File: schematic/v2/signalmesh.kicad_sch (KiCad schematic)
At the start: 37 parts, among them J13 UUM_DBG, U21 74HC4050D, U22 AP2112K-3.3, U23 W25Q128JVS, U24 74HC4050D, U25 AP2112K-3.3, U26 W25Q128JVS, U27 MCP2551-I-P, U28 74LVC1G3157, U29 MCP2551-I-P, U3 NUCLEO-F303RE, U30 MCP2551-I-P, U31 MCP2551-I-P

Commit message: no errors in the ERC!
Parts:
- removed C10: 0.1uf, Capacitor_SMD:C_0805_2012Metric, symbol Device:C_Small
- removed C8, C9: 10uf, Capacitor_SMD:C_0805_2012Metric, symbol Device:C_Small
- removed D25, D26, D27, D28: LED_PWR, LED_SMD:LED_0603_1608Metric, symbol Device:LED
- removed D29: LED_OK, LED_SMD:LED_0603_1608Metric, symbol Device:LED
- removed D30: LED_FAIL, LED_SMD:LED_0603_1608Metric, symbol Device:LED
- removed D31: LED_WARN, LED_SMD:LED_0603_1608Metric, symbol Device:LED
- removed J13: UUM_DBG, Connector_PinHeader_1.00mm:PinHeader_1x03_P1.00mm_Horizontal, symbol Connector_Generic:Conn_01x03
- removed R10, R43, R45, R46, R48, R49, R9: 300, Resistor_SMD:R_0805_2012Metric_Pad1.20x1.40mm_HandSolder, symbol Device:R
- removed R42: 100, Resistor_SMD:R_0805_2012Metric_Pad1.20x1.40mm_HandSolder, symbol Device:R
- removed U21, U24: 74HC4050D, 74HC4050D:SO16, symbol 74HC4050D:74HC4050D
- removed U22, U25: AP2112K-3.3, Package_TO_SOT_SMD:SOT-23-5, symbol Regulator_Linear:AP2112K-3.3
- removed U23, U26: W25Q128JVS, Package_SO:SOIC-8_5.3x5.3mm_P1.27mm, symbol Memory_Flash:W25Q128JVS
- removed U28: 74LVC1G3157, SN74LVC1G3157:SC70-6, symbol 74xGxx:74LVC1G3157
- removed U3: NUCLEO-F303RE, NUCLEO-F303RE:ST_NUCLEO-F303RE, symbol NUCLEO-F303RE:NUCLEO-F303RE
- added R73, R74, R75, R76: 10k, Resistor_SMD:R_0805_2012Metric_Pad1.20x1.40mm_HandSolder, symbol Device:R
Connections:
- net VDD_UUM is gone; now on net UUM_VDD: U27.3 (VDD)
- net GND: now also R73.2, R74.2, R75.2, R76.2
- net at U31.8 (Rs): now also R76.1
- net at U27.8 (Rs): now also R73.1
- net at U29.8 (Rs): now also R74.1
- net at U30.8 (Rs): now also R75.1
- net VDD_APM renamed APM_VDD
- net VDD_DSM renamed DSM_VDD
- net VDD_TDM renamed TDM_VDD
- no-connect marks 0 -> 4
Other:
- added sheet UUM (UUM.kicad_sch)
- sheet TDM ports: added 7SDD_VDD, APM_VDD, DSM_VDD, TDM_VDD, UUM_VDD; removed none
- note removed: "UUM writes to both SPI flashes at once but can only read from 1 at a time via a GPIO-ctrl'd switch"
- note removed: "Upload & Update Module"
- note removed: "W25Q128 UUM #1"
- note removed: "W25Q128 UUM #2"
- moved on the sheet: H1, H2, H5, H6, R44, R47, U27, U29, U30, U31

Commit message: attempting new PCB layout
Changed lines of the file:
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@@
 	(wire
 		(pts
-			(xy 185.42 186.69) (xy 198.12 186.69)
+			(xy 102.87 185.42) (xy 115.57 185.42)
 		)
 		(stroke
@@
 	(wire
 		(pts
-			(xy 185.42 208.28) (xy 198.12 208.28)
+			(xy 181.61 165.1) (xy 194.31 165.1)
 		)
 		(stroke
@@
 	(wire
 		(pts
-			(xy 185.42 184.15) (xy 198.12 184.15)
+			(xy 102.87 182.88) (xy 115.57 182.88)
 		)
 		(stroke
@@
 	(wire
 		(pts
-			(xy 185.42 210.82) (xy 198.12 210.82)
+			(xy 181.61 167.64) (xy 194.31 167.64)
 		)
 		(stroke
@@
 	)
 	(label "TDM_CAN_RD"
-		(at 185.42 184.15 0)
+		(at 102.87 182.88 0)
 		(effects
 			(font
@@
 	)
 	(label "UUM_CAN_RD"
-		(at 185.42 208.28 0)
+		(at 181.61 165.1 0)
 		(effects
 			(font
@@
 	)
 	(label "UUM_CAN_TD"
-		(at 185.42 210.82 0)
+		(at 181.61 167.64 0)
 		(effects
 			(font
@@
 	)
 	(label "TDM_CAN_TD"
-		(at 185.42 186.69 0)
+		(at 102.87 185.42 0)
 		(effects
 			(font
@@
 	)
 	(sheet
-		(at 198.12 162.56)
-		(size 31.75 27.94)
+		(at 115.57 161.29)
+		(size 38.1 27.94)
 		(exclude_from_sim no)
 		(in_bom yes)
@@
 		)
 		(property "Sheetname" "TDM"
-			(at 198.12 161.8484 0)
+			(at 115.57 160.5784 0)
 			(effects
 				(font
@@
 		)
 		(property "Sheetfile" "TDM.kicad_sch"
-			(at 198.12 191.0846 0)
+			(at 115.57 189.8146 0)
 			(effects
 				(font
@@
 		)
 		(property "Field2" ""
-			(at 198.12 162.56 0)
+			(at 115.57 161.29 0)
 			(effects
 				(font
@@
 		)
 		(pin "TDM_CAN_TD" output
-			(at 198.12 186.69 180)
+			(at 115.57 185.42 180)
 			(effects
 				(font
@@
 		)
 		(pin "TDM_CAN_RD" input
-			(at 198.12 184.15 180)
+			(at 115.57 182.88 180)
 			(effects
 				(font
@@
 		)
 		(pin "UUM_VDD" output
-			(at 229.87 179.07 0)
+			(at 153.67 177.8 0)
 			(effects
 				(font
@@
 		)
 		(pin "ACM_VDD" output
-			(at 229.87 168.91 0)
+			(at 153.67 167.64 0)
 			(effects
 				(font
@@
 		)
 		(pin "7SDD_VDD" output
-			(at 229.87 166.37 0)
+			(at 153.67 165.1 0)
 			(effects
 				(font
@@
 		)
 		(pin "TDM_VDD" output
-			(at 229.87 176.53 0)
+			(at 153.67 175.26 0)
 			(effects
 				(font
@@
 		)
 		(pin "APM_VDD" output
-			(at 229.87 171.45 0)
+			(at 153.67 170.18 0)
 			(effects
 				(font
@@
 		)
 		(pin "DSM_VDD" output
-			(at 229.87 173.99 0)
+			(at 153.67 172.72 0)
 			(effects
 				(font
@@
 	)
 	(sheet
-		(at 198.12 204.47)
-		(size 31.75 12.7)
+		(at 194.31 161.29)
+		(size 38.1 27.94)
 		(exclude_from_sim no)
 		(in_bom yes)
@@
 		)
 		(property "Sheetname" "UUM"
-			(at 198.12 203.7584 0)
+			(at 194.31 160.5784 0)
 			(effects
 				(font
@@
 		)
 		(property "Sheetfile" "UUM.kicad_sch"
-			(at 198.12 217.7546 0)
+			(at 194.31 189.8146 0)
 			(effects
 				(font
@@
 		)
 		(pin "UUM_CAN_RD" input
-			(at 198.12 208.28 180)
+			(at 194.31 165.1 180)
 			(effects
 				(font
@@
 		)
 		(pin "UUM_CAN_TD" output
-			(at 198.12 210.82 180)
+			(at 194.31 167.64 180)
 			(effects
 				(font

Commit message: time to start routing?
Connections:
- no-connect marks 4 -> 9
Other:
- added sheet USB_debug_ACM (USB_debug.kicad_sch)
- added sheet USB_debug_APM (USB_debug.kicad_sch)
- added sheet USB_debug_DSM (USB_debug.kicad_sch)
- added sheet USB_debug_TDM (USB_debug.kicad_sch)
- added sheet USB_debug_UUM (USB_debug.kicad_sch)
- sheet ACM ports: added ACM_DBG_RX, ACM_DBG_TX, ACM_VDD; removed none
- sheet APM ports: added APM_DBG_RX, APM_DBG_TX, APM_VDD; removed none
- sheet DSM ports: added DSM_DBG_RX, DSM_DBG_TX, DSM_VDD; removed none
- sheet TDM ports: added TDM_DBG_RX, TDM_DBG_TX; removed none
- sheet UUM ports: added UUM_DBG_RX, UUM_DBG_TX, UUM_VDD; removed none
- moved on the sheet: R44, R47, R73, R74, R75, R76, U27, U29, U30, U31

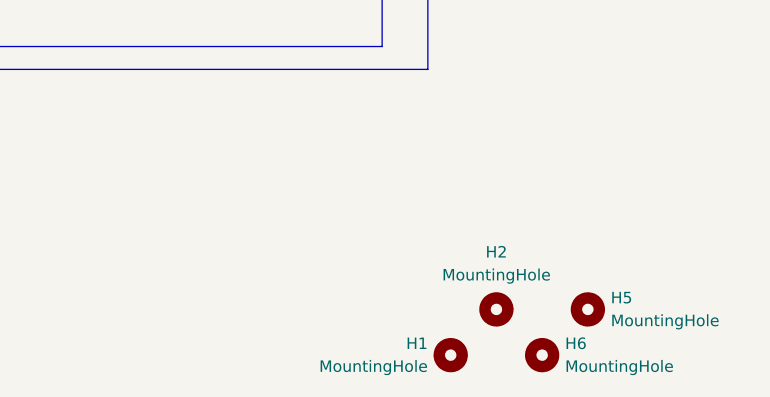
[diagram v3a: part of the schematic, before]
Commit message: gonna throw auto route on. I think I have enough put together for now
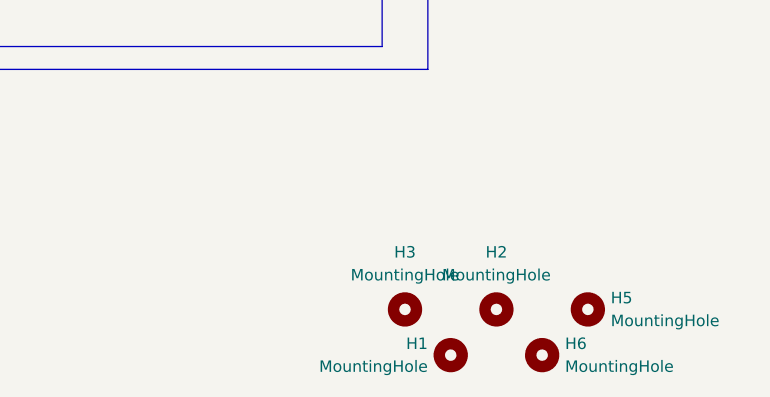
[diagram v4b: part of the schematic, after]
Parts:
- added H3: MountingHole, MountingHole:MountingHole_3.2mm_M3, symbol Mechanical:MountingHole
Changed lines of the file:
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@@
+	)
+	(symbol
+		(lib_id "Mechanical:MountingHole")
+		(at 372.11 243.84 0)
+		(unit 1)
+		(exclude_from_sim no)
+		(in_bom no)
+		(on_board yes)
+		(dnp no)
+		(fields_autoplaced yes)
+		(property "Reference" "H3"
+			(at 372.11 237.49 0)
+			(effects
+				(font
+					(size 1.27 1.27)
+				)
+			)
+		)
+		(property "Value" "MountingHole"
+			(at 372.11 240.03 0)
+			(effects
+				(font
+					(size 1.27 1.27)
+				)
+			)
+		)
+		(property "Footprint" "MountingHole:MountingHole_3.2mm_M3"
+			(at 372.11 243.84 0)
+			(effects
+				(font
+					(size 1.27 1.27)
+				)
+				(hide yes)
+			)
+		)
+		(property "Datasheet" "~"
+			(at 372.11 243.84 0)
+			(effects
+				(font
+					(size 1.27 1.27)
+				)
+				(hide yes)
+			)
+		)
+		(property "Description" "Mounting Hole without connection"
+			(at 372.11 243.84 0)
+			(effects
+				(font
+					(size 1.27 1.27)
+				)
+				(hide yes)
+			)
+		)
+		(instances
+			(project "signalmesh"
+				(path "/fe7b15e9-f0ed-4338-9f03-dd7651dace13"
+					(reference "H3")
+					(unit 1)
+				)
+			)
+		)
 	)
 	(symbol

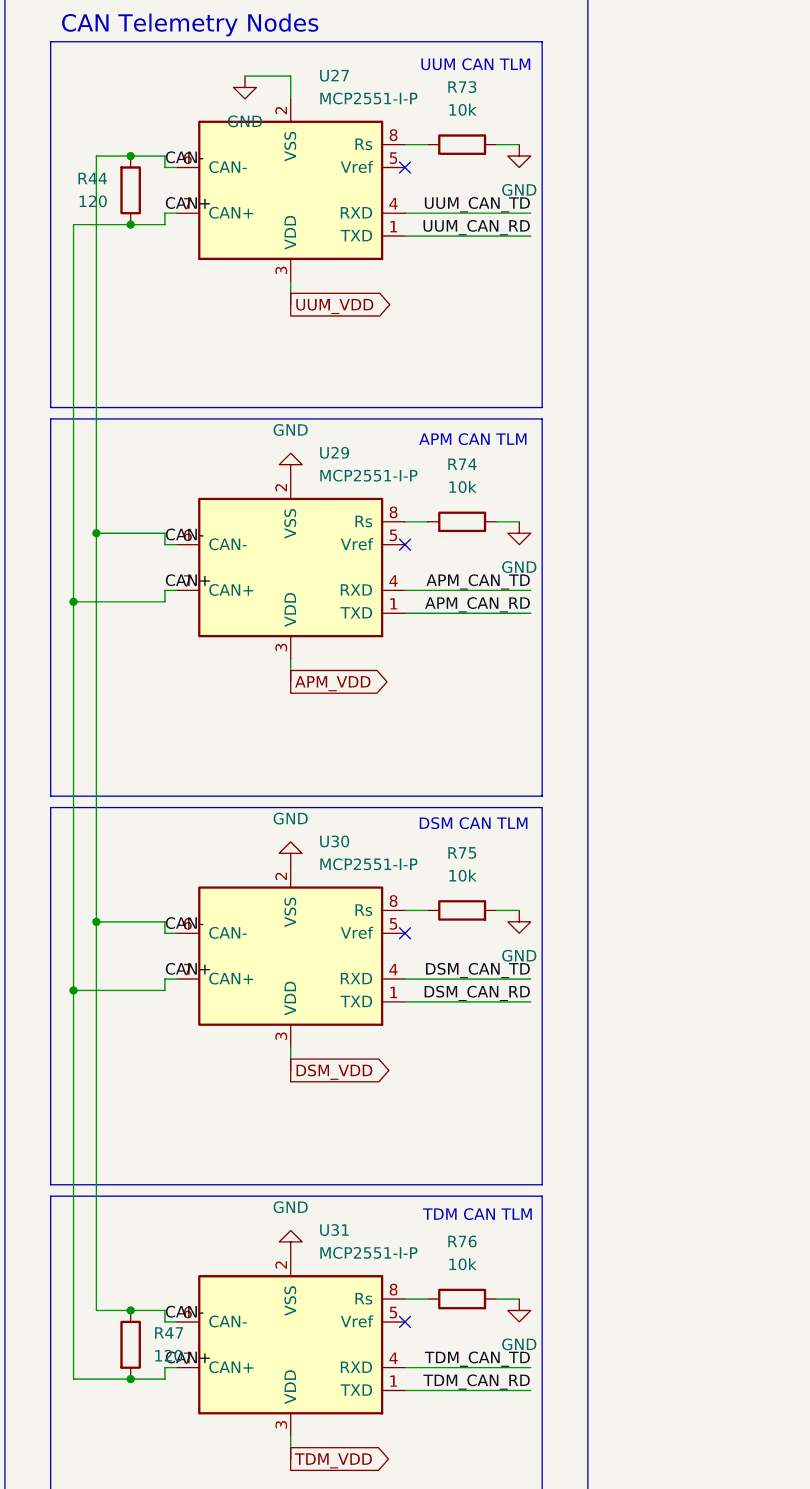
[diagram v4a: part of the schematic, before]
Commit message: fixed designators
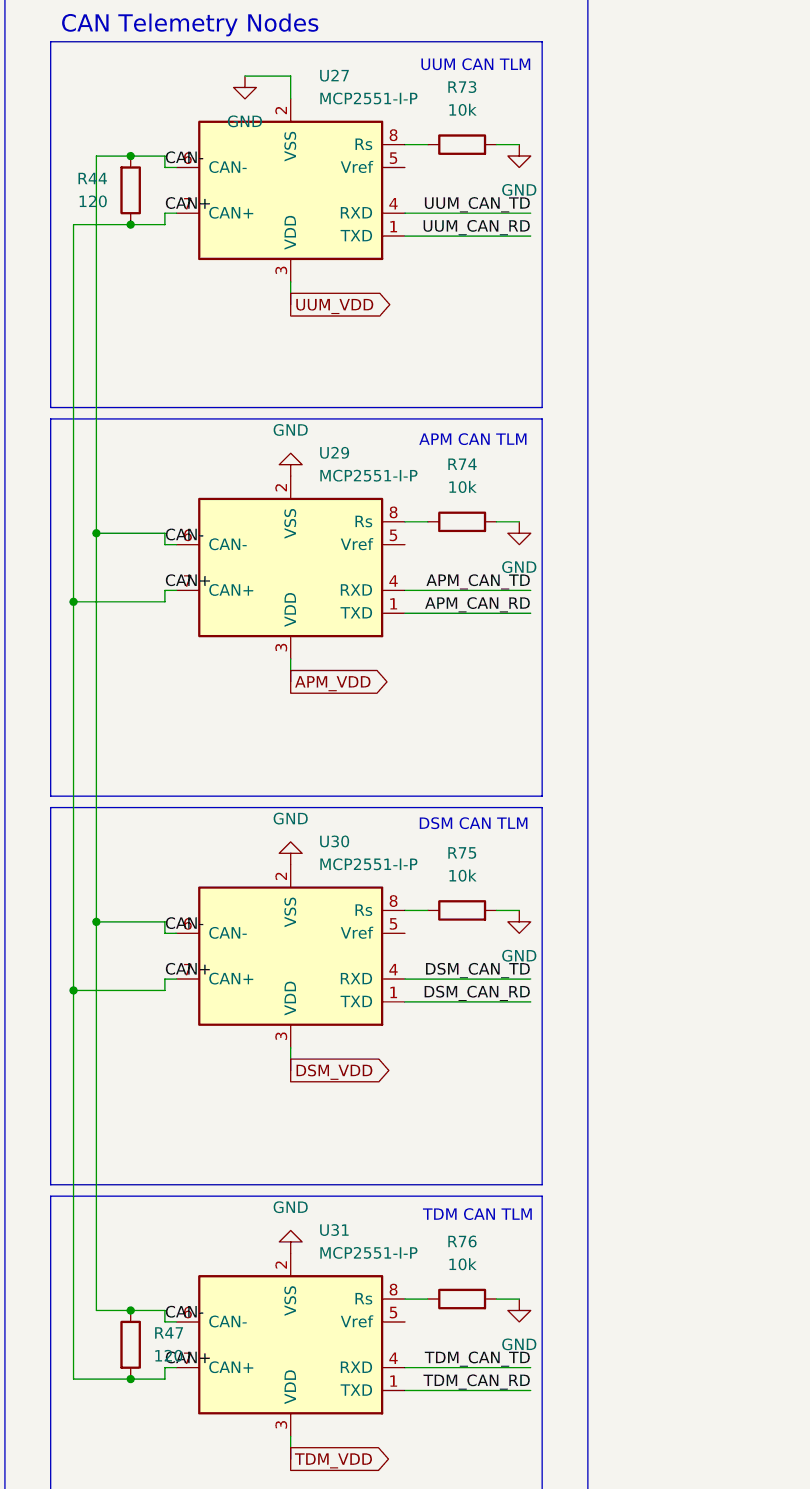
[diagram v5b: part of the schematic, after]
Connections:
- no-connect marks 9 -> 5
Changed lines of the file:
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@@
-	)
-	(no_connect
-		(at 354.33 100.33)
-	)
-	(no_connect
-		(at 354.33 143.51)
 	)
 	(no_connect
@@
 	)
 	(no_connect
-		(at 354.33 186.69)
-	)
-	(no_connect
-		(at 354.33 58.42)
-	)
-	(no_connect

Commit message: hmmm figuring out filter module right now
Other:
- added sheet AFFM (AFFM.kicad_sch)

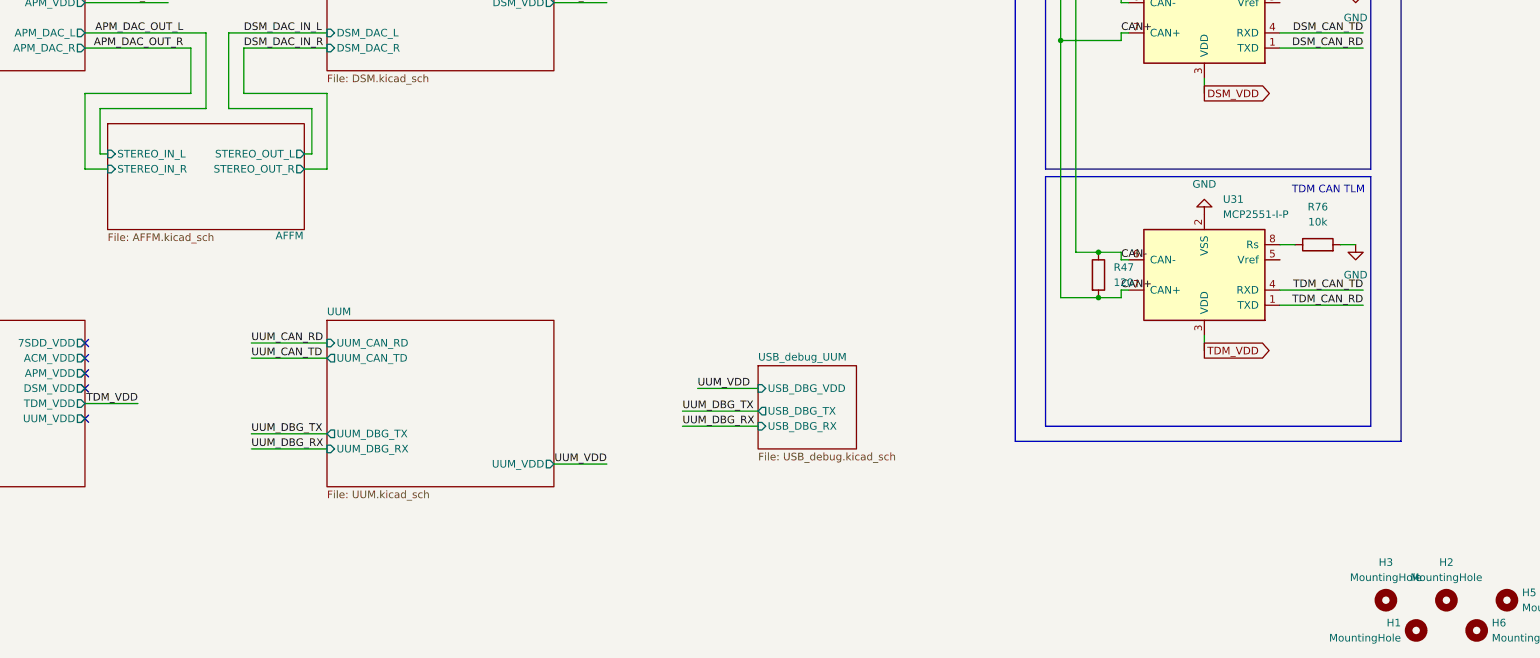
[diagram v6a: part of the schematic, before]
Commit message: dip switch for multi pole filter? this is all for experimenting for now, a refined design with less togleables will come later
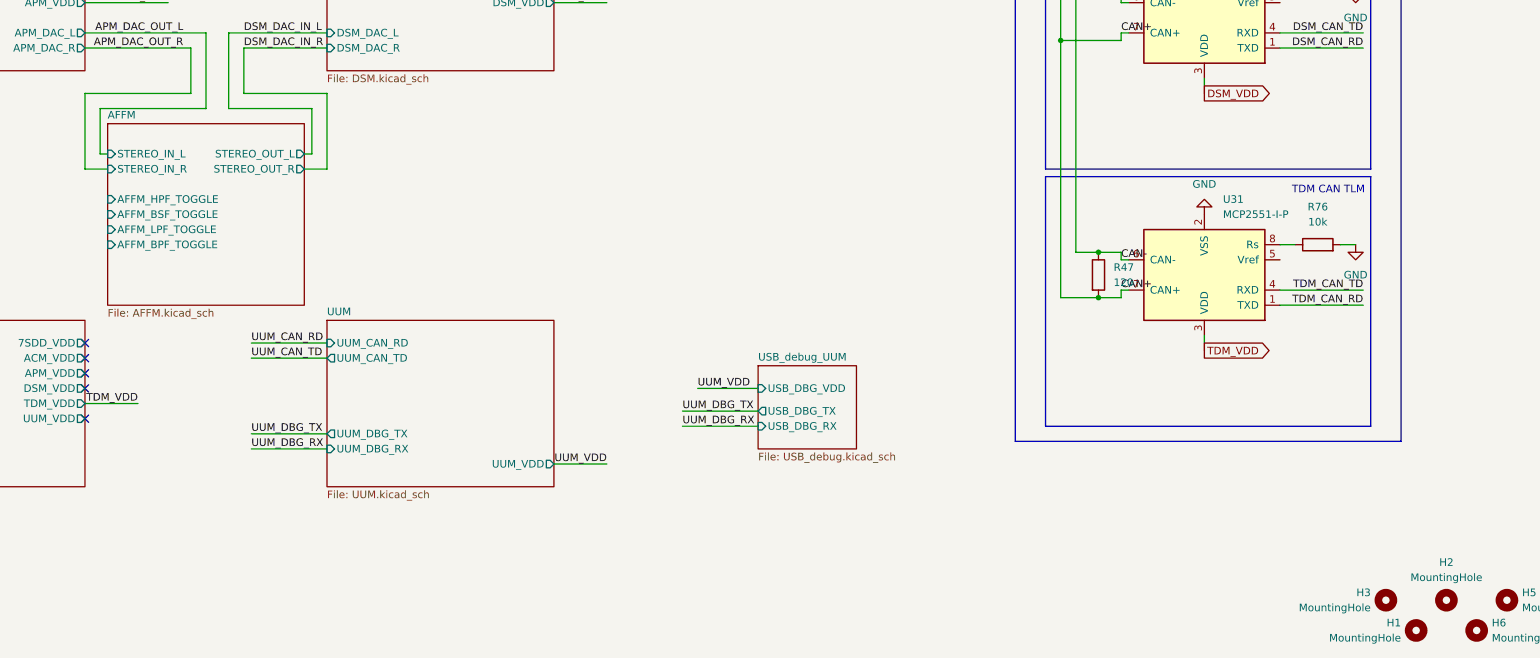
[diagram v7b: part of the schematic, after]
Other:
- sheet AFFM ports: added AFFM_BPF_TOGGLE, AFFM_BSF_TOGGLE, AFFM_HPF_TOGGLE, AFFM_LPF_TOGGLE; removed none
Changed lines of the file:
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@@
 		(fields_autoplaced yes)
 		(property "Reference" "H3"
-			(at 372.11 237.49 0)
-			(effects
-				(font
-					(size 1.27 1.27)
-				)
+			(at 369.57 242.5699 0)
+			(effects
+				(font
+					(size 1.27 1.27)
+				)
+				(justify right)
 			)
 		)
 		(property "Value" "MountingHole"
-			(at 372.11 240.03 0)
-			(effects
-				(font
-					(size 1.27 1.27)
-				)
+			(at 369.57 245.1099 0)
+			(effects
+				(font
+					(size 1.27 1.27)
+				)
+				(justify right)
 			)
 		)
@@
 			(project "signalmesh"
 				(path "/fe7b15e9-f0ed-4338-9f03-dd7651dace13"
-					(page "2")
+					(page "23")
 				)
 			)
@@
 			(project "signalmesh"
 				(path "/fe7b15e9-f0ed-4338-9f03-dd7651dace13"
-					(page "19")
+					(page "24")
 				)
 			)
@@
 	(sheet
 		(at 157.48 163.83)
-		(size 33.02 17.78)
+		(size 33.02 30.48)
 		(exclude_from_sim no)
 		(in_bom yes)
 		(on_board yes)
 		(dnp no)
+		(fields_autoplaced yes)
 		(stroke
 			(width 0.1524)
@@
 		)
 		(property "Sheetname" "AFFM"
-			(at 185.674 183.388 0)
+			(at 157.48 163.1184 0)
 			(effects
 				(font
@@
 		)
 		(property "Sheetfile" "AFFM.kicad_sch"
-			(at 157.48 182.1946 0)
+			(at 157.48 194.8946 0)
 			(effects
 				(font
@@
 			(effects
 				(font
+					(size 1.27 1.27)
+				)
+				(justify left)
+			)
+		)
+		(pin "AFFM_HPF_TOGGLE" input
+			(at 157.48 176.53 180)
+			(effects
+				(font
+					(size 1.27 1.27)
+				)
+				(justify left)
+			)
+		)
+		(pin "AFFM_BSF_TOGGLE" input
+			(at 157.48 179.07 180)
+			(effects
+				(font
+					(size 1.27 1.27)
+				)
+				(justify left)
+			)
+		)
+		(pin "AFFM_LPF_TOGGLE" input
+			(at 157.48 181.61 180)
+			(effects
+				(font
+					(size 1.27 1.27)
+				)
+				(justify left)
+			)
+		)
+		(pin "AFFM_BPF_TOGGLE" input
+			(at 157.48 184.15 180)
+			(effects
+				(font
